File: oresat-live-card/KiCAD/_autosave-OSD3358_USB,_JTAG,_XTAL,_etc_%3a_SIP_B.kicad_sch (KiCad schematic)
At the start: 97 parts, among them J10 SM06B-SRSS-TB(LF)(SN), J8 FTSH-105-XX-X-DV-K, U1 RCLAMP0504FB, U20 TPS2041BQDBVRQ1, U7 OSD3358-512M-BSM, U9 TPS2041BQDBVRQ1, Y1 24MHz, Y2 ABS07-32.768KHZ-T, Y3 6MHz

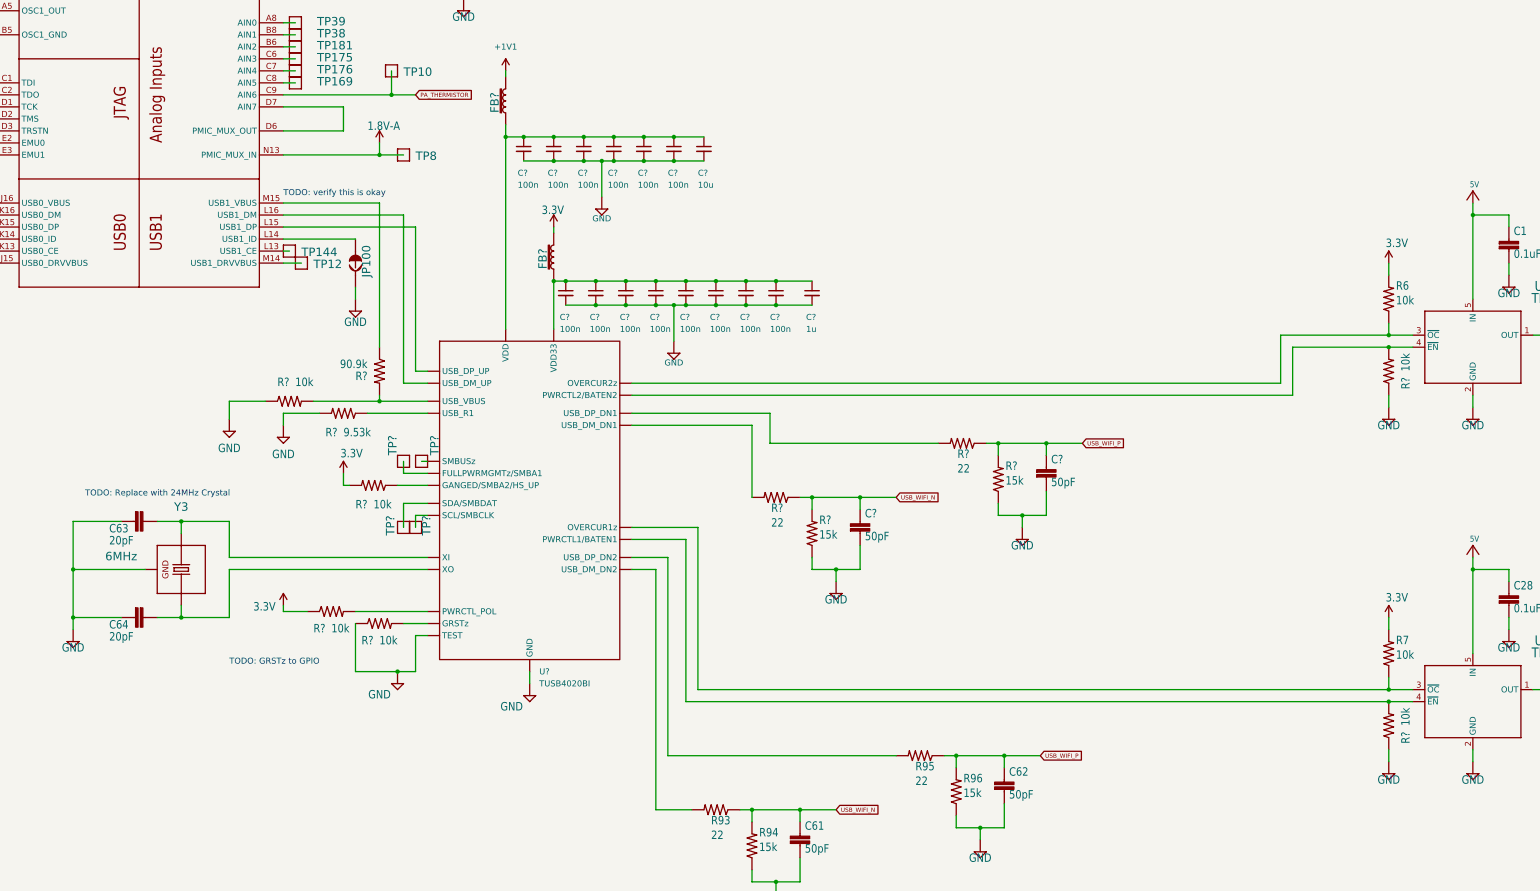
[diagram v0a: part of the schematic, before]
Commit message: Schematic update for V1.2, still a few outstanding TODOs
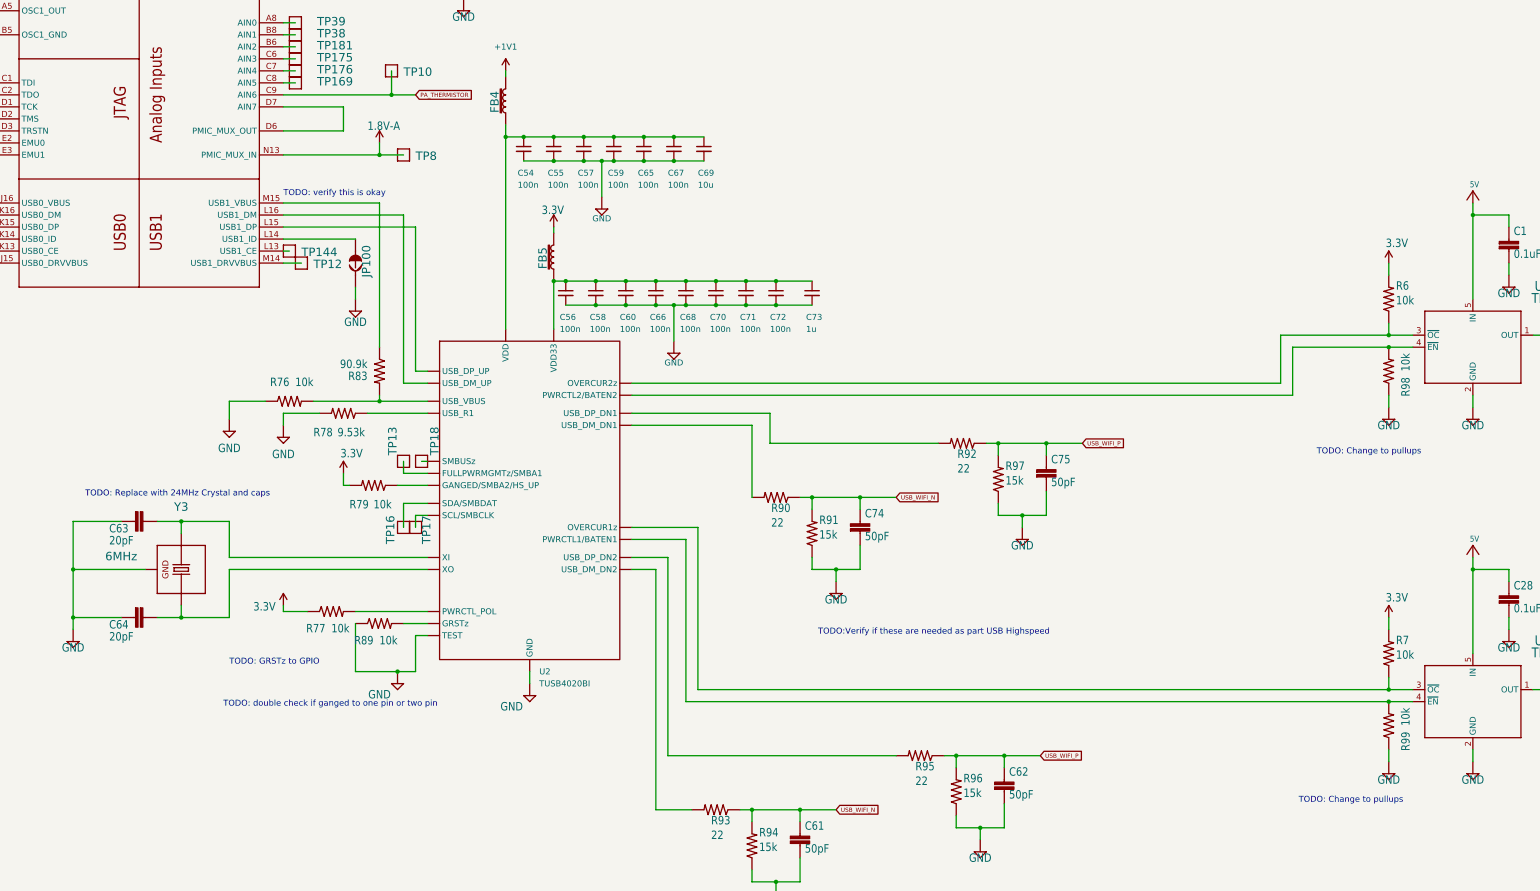
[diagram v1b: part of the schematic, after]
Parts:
- gave numbers to parts that had none: 37
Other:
- note added: "TODO: Change to pullups"
- note added: "TODO: Replace with 24MHz Crystal and caps"
- note added: "TODO: double check if ganged to one pin or two pin"
- note added: "TODO:Verify if these are needed as part USB Highspeed"
- note removed: "TODO: Replace with 24MHz Crystal"
